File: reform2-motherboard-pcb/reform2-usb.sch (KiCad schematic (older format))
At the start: 85 parts, among them J14 USB_INT2, J17 USB3_A, J5 USB3_A, J6 USB3_A, J9 USB_INT1, U15 TPS2561, U16 TPS2561, U9 TUSB8041IPAPRQ1, Y1 24MHz

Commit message: reform2-motherboard: version D-4 finished; fixes critical D-3 bugs; adds PCIe refclk termination, speaker output filter stage, pcie0 3v3 load switch, imx reset line to lpc, charge current control line to lpc
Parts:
- removed R100, R101, R82, R83, R88, R89, R94, R95: 0, Resistor_SMD:R_0603_1608Metric, symbol Device:R_Small
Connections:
- net USB3_1_EN: now also U15.5 (EN2)
- net USB3_1_OVERCURn: now also U15.6 (~FAULT2)
- net USB3_2_EN: now also U15.4 (EN1)
- net USB3_2_OVERCURn: now also U15.10 (~FAULT1)
- net USB3_3_EN: now also U16.5 (EN2)
- net USB3_3_OVERCURn: now also U16.6 (~FAULT2)
- net USB3_4_EN: now also U16.4 (EN1)
- net USB3_4_OVERCURn: now also U16.10 (~FAULT1)
- net +1V1 renamed +1V2
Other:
- note removed: "FIXME: this goes nowhere"
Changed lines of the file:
@@
 Sheet 8 9
 Title "MNT Reform 2 USB"
-Date "2020-04-11"
+Date "2020-05-19"
 Rev "2.0D-4"
 Comp "MNT Research GmbH"
@@
 	9600 1600 9900 1600
 Connection ~ 9900 1600
-$Comp
-L power:+1V1 #PWR035
-U 1 1 5D9F2CBF
-P 15450 1750
-F 0 "#PWR035" H 15450 1600 50  0001 C CNN
-F 1 "+1V1" H 15465 1923 50  0000 C CNN
-F 2 "" H 15450 1750 50  0001 C CNN
-F 3 "" H 15450 1750 50  0001 C CNN
-	1    15450 1750
-	1    0    0    -1
-$EndComp
 Wire Wire Line
 	11800 2300 11900 2300
@@
 	13050 1400 13050 1750
 Wire Wire Line
-	15450 1750 15450 1800
-Wire Wire Line
 	13050 1150 13050 1200
 Wire Wire Line
@@
 Text GLabel 7050 5900 2    50   Input ~ 0
 USB_PWR
-$Comp
-L Device:R_Small R89
-U 1 1 5DA29AEA
-P 3000 1900
-F 0 "R89" V 2900 1900 50  0000 C CNN
-F 1 "0" V 3000 1900 50  0000 C CNN
-F 2 "Resistor_SMD:R_0603_1608Metric" H 3000 1900 50  0001 C CNN
-F 3 "~" H 3000 1900 50  0001 C CNN
-F 4 "Vishay Dale" H 3000 1900 50  0001 C CNN "Manufacturer"
-F 5 "CRCW06030000Z0EAC" H 3000 1900 50  0001 C CNN "Manufacturer_No"
-F 6 "Mouser" H 3000 1900 50  0001 C CNN "Distributor"
-F 7 "y" H 3000 1900 50  0001 C CNN "Checked"
-	1    3000 1900
-	0    -1   -1   0
-$EndComp
-$Comp
-L Device:R_Small R88
-U 1 1 5DA2A4B1
-P 3000 1600
-F 0 "R88" V 2900 1600 50  0000 C CNN
-F 1 "0" V 3000 1600 50  0000 C CNN
-F 2 "Resistor_SMD:R_0603_1608Metric" H 3000 1600 50  0001 C CNN
-F 3 "~" H 3000 1600 50  0001 C CNN
-F 4 "Vishay Dale" H 3000 1600 50  0001 C CNN "Manufacturer"
-F 5 "CRCW06030000Z0EAC" H 3000 1600 50  0001 C CNN "Manufacturer_No"
-F 6 "Mouser" H 3000 1600 50  0001 C CNN "Distributor"
-F 7 "y" H 3000 1600 50  0001 C CNN "Checked"
-	1    3000 1600
-	0    -1   -1   0
-$EndComp
-$Comp
-L Device:R_Small R100
-U 1 1 5DA2A6C7
-P 6500 1600
-F 0 "R100" V 6400 1600 50  0000 C CNN
-F 1 "0" V 6500 1600 50  0000 C CNN
-F 2 "Resistor_SMD:R_0603_1608Metric" H 6500 1600 50  0001 C CNN
-F 3 "~" H 6500 1600 50  0001 C CNN
-F 4 "Vishay Dale" H 6500 1600 50  0001 C CNN "Manufacturer"
-F 5 "CRCW06030000Z0EAC" H 6500 1600 50  0001 C CNN "Manufacturer_No"
-F 6 "Mouser" H 6500 1600 50  0001 C CNN "Distributor"
-F 7 "y" H 6500 1600 50  0001 C CNN "Checked"
-	1    6500 1600
-	0    -1   -1   0
-$EndComp
-$Comp
-L Device:R_Small R101
-U 1 1 5DA2AAEE
-P 6500 1900
-F 0 "R101" V 6400 1900 50  0000 C CNN
-F 1 "0" V 6500 1900 50  0000 C CNN
-F 2 "Resistor_SMD:R_0603_1608Metric" H 6500 1900 50  0001 C CNN
-F 3 "~" H 6500 1900 50  0001 C CNN
-F 4 "Vishay Dale" H 6500 1900 50  0001 C CNN "Manufacturer"
-F 5 "CRCW06030000Z0EAC" H 6500 1900 50  0001 C CNN "Manufacturer_No"
-F 6 "Mouser" H 6500 1900 50  0001 C CNN "Distributor"
-F 7 "y" H 6500 1900 50  0001 C CNN "Checked"
-	1    6500 1900
-	0    -1   -1   0
-$EndComp
 Text GLabel 13500 3500 2    50   Input ~ 0
 USB3_1_OVERCURn
@@
 Text GLabel 13500 6200 2    50   Input ~ 0
 USB3_4_OVERCURn
-Text GLabel 3100 1900 2    50   Output ~ 0
+Text GLabel 2900 1900 2    50   Output ~ 0
 USB3_1_OVERCURn
-Text GLabel 3100 1600 2    50   Output ~ 0
+Text GLabel 2900 1600 2    50   Output ~ 0
 USB3_2_OVERCURn
 Text GLabel 2100 6700 2    50   Output ~ 0
@@
 Wire Wire Line
 	5700 2450 5700 2400
-Wire Wire Line
-	1450 1800 1700 1800
-Wire Wire Line
-	1700 1900 1450 1900
 $Comp
 L Device:C_Small C66
@@
 Wire Wire Line
 	1550 6200 1800 6200
-Text GLabel 6600 1900 2    50   Output ~ 0
+Text GLabel 6400 1900 2    50   Output ~ 0
 USB3_3_OVERCURn
-Text GLabel 6600 1600 2    50   Output ~ 0
+Text GLabel 6400 1600 2    50   Output ~ 0
 USB3_4_OVERCURn
 $Comp
@@
 	10300 5200 10900 5200
 Wire Wire Line
-	5200 1800 4800 1800
-Wire Wire Line
-	4800 1900 5200 1900
-Wire Wire Line
 	4900 2200 4900 1600
 Connection ~ 4900 1600
@@
 	4900 2450 4900 2400
 Connection ~ 5700 2450
-$Comp
-L Device:R_Small R82
-U 1 1 5DC331BA
-P 1350 1800
-F 0 "R82" V 1250 1800 50  0000 C CNN
-F 1 "0" V 1350 1800 50  0000 C CNN
-F 2 "Resistor_SMD:R_0603_1608Metric" H 1350 1800 50  0001 C CNN
-F 3 "~" H 1350 1800 50  0001 C CNN
-F 4 "Vishay Dale" H 1350 1800 50  0001 C CNN "Manufacturer"
-F 5 "CRCW06030000Z0EAC" H 1350 1800 50  0001 C CNN "Manufacturer_No"
-F 6 "Mouser" H 1350 1800 50  0001 C CNN "Distributor"
-F 7 "y" H 1350 1800 50  0001 C CNN "Checked"
-	1    1350 1800
-	0    1    1    0
-$EndComp
-Wire Wire Line
-	1250 1800 1200 1800
-$Comp
-L Device:R_Small R83
-U 1 1 5DC3CB0C
-P 1350 1900
-F 0 "R83" V 1250 1900 50  0000 C CNN
-F 1 "0" V 1350 1900 50  0000 C CNN
-F 2 "Resistor_SMD:R_0603_1608Metric" H 1350 1900 50  0001 C CNN
-F 3 "~" H 1350 1900 50  0001 C CNN
-F 4 "Vishay Dale" H 1350 1900 50  0001 C CNN "Manufacturer"
-F 5 "CRCW06030000Z0EAC" H 1350 1900 50  0001 C CNN "Manufacturer_No"
-F 6 "Mouser" H 1350 1900 50  0001 C CNN "Distributor"
-F 7 "y" H 1350 1900 50  0001 C CNN "Checked"
-	1    1350 1900
-	0    -1   -1   0
-$EndComp
-Wire Wire Line
-	1250 1900 1200 1900
-$Comp
-L Device:R_Small R94
-U 1 1 5DC58706
-P 4700 1800
-F 0 "R94" V 4600 1800 50  0000 C CNN
-F 1 "0" V 4700 1800 50  0000 C CNN
-F 2 "Resistor_SMD:R_0603_1608Metric" H 4700 1800 50  0001 C CNN
-F 3 "~" H 4700 1800 50  0001 C CNN
-F 4 "Vishay Dale" H 4700 1800 50  0001 C CNN "Manufacturer"
-F 5 "CRCW06030000Z0EAC" H 4700 1800 50  0001 C CNN "Manufacturer_No"
-F 6 "Mouser" H 4700 1800 50  0001 C CNN "Distributor"
-F 7 "y" H 4700 1800 50  0001 C CNN "Checked"
-	1    4700 1800
-	0    1    1    0
-$EndComp
-$Comp
-L Device:R_Small R95
-U 1 1 5DC58710
-P 4700 1900
-F 0 "R95" V 4600 1900 50  0000 C CNN
-F 1 "0" V 4700 1900 50  0000 C CNN
-F 2 "Resistor_SMD:R_0603_1608Metric" H 4700 1900 50  0001 C CNN
-F 3 "~" H 4700 1900 50  0001 C CNN
-F 4 "Vishay Dale" H 4700 1900 50  0001 C CNN "Manufacturer"
-F 5 "CRCW06030000Z0EAC" H 4700 1900 50  0001 C CNN "Manufacturer_No"
-F 6 "Mouser" H 4700 1900 50  0001 C CNN "Distributor"
-F 7 "y" H 4700 1900 50  0001 C CNN "Checked"
-	1    4700 1900
-	0    -1   -1   0
-$EndComp
-Wire Wire Line
-	4600 1800 4550 1800
-Wire Wire Line
-	4550 1900 4600 1900
 $Comp
 L Device:R_Small R98
@@
 Text Notes 8400 4900 0    50   ~ 0
 TODO: hook up SCL/SDA?
-Text Notes 15000 1200 0    50   ~ 0
-FIXME: this goes nowhere
+$Comp
+L power:+1V2 #PWR0216
+U 1 1 5ECB605D
+P 15450 1700
+F 0 "#PWR0216" H 15450 1550 50  0001 C CNN
+F 1 "+1V2" H 15465 1873 50  0000 C CNN
+F 2 "" H 15450 1700 50  0001 C CNN
+F 3 "" H 15450 1700 50  0001 C CNN
+	1    15450 1700
+	1    0    0    -1
+$EndComp
+Wire Wire Line
+	15450 1700 15450 1800
+Wire Wire Line
+	4550 1800 5200 1800
+Wire Wire Line
+	4550 1900 5200 1900
+Wire Wire Line
+	1200 1800 1700 1800
+Wire Wire Line
+	1200 1900 1700 1900
 $EndSCHEMATC

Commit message: reform2-motherboard: first R-1 snapshot. main changes: EMI, ESD, audio filter, enable FETs, SHDN fix, more rail switches
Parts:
- added C164, C167: 10uF, Capacitor_SMD:C_0603_1608Metric, symbol Device:C_Small
- added R2, R83: 10k, Resistor_SMD:R_0603_1608Metric, symbol Device:R_Small
- added U21, U25, U26: SP3012-06UTG, footprints:SON50P350X135X55-14N, symbol reform2:SP3012-06UTG
- added U24, U27: AP22815, footprints:TSOT-25, symbol reform2:AP22815
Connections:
- net +3V3: now also C167.1, R2.2, U27.5 (IN); no longer FB1.1
- net +5V: now also C164.1, R83.2, U24.5 (IN); no longer C43.1, C66.1, C73.1, FB8.1, R61.2, U15.2 (IN), U15.3 (IN), U16.2 (IN), U16.3 (IN)
- net GND: now also C164.2, C167.2, U21.10, U21.5, U24.2 (GND), U25.10, U25.5, U26.10, U26.5, U27.2 (GND)
- net USB2_DN: now also U21.12, U21.3
- net USB2_DP: now also U21.11, U21.4
- net USB2_RX_N: now also U21.7, U21.8
- net USB2_RX_P: now also U21.6, U21.9
- net USB2_TX_N: now also U21.13, U21.2
- net USB2_TX_P: now also U21.1, U21.14
- net USB3_1_DN: now also U25.12, U25.3
- net USB3_1_DP: now also U25.11, U25.4
- net USB3_1_SSRXN: now also U25.7, U25.8
- net USB3_1_SSRXP: now also U25.6, U25.9
- net USB3_2_DN: now also U26.12, U26.3
- net USB3_2_DP: now also U26.11, U26.4
- net USB3_2_SSRXN: now also U26.7, U26.8
- net USB3_2_SSRXP: now also U26.6, U26.9
- net USB3_1_SSTXCN: now reaches C40.2, J6.8 (SSTX-)
- net USB3_1_SSTXCN: now also U25.13, U25.2
- net USB3_1_SSTXCP: now reaches C42.2, J6.9 (SSTX+)
- net USB3_1_SSTXCP: now also U25.1, U25.14
- net USB3_2_SSTXCN: now reaches C39.2, J5.8 (SSTX-)
- net USB3_2_SSTXCN: now also U26.13, U26.2
- net USB3_2_SSTXCP: now reaches C41.2, J5.9 (SSTX+)
- net USB3_2_SSTXCP: now also U26.1, U26.14
- new net: R83.1, U24.3 (FLG)
- new net: R2.1, U27.3 (FLG)
- new net 3V3_PWR_AUX: FB1.1, U27.1 (OUT)
- new net AUX_PWR_EN: U27.4 (EN)
- new net USB_PWR: C43.1, C66.1, C73.1, FB8.1, R61.2, U15.2 (IN), U15.3 (IN), U16.2 (IN), U16.3 (IN), U24.1 (OUT)
- new net USB_PWR_EN: U24.4 (EN)
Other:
- note added: "TODO: RESETn pulldown"
- note removed: "TODO: consider ESD7016"
- moved on the sheet: C39, C40, C41, C42, C43, C69, C71, C75, C76, C77, C79, FB6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

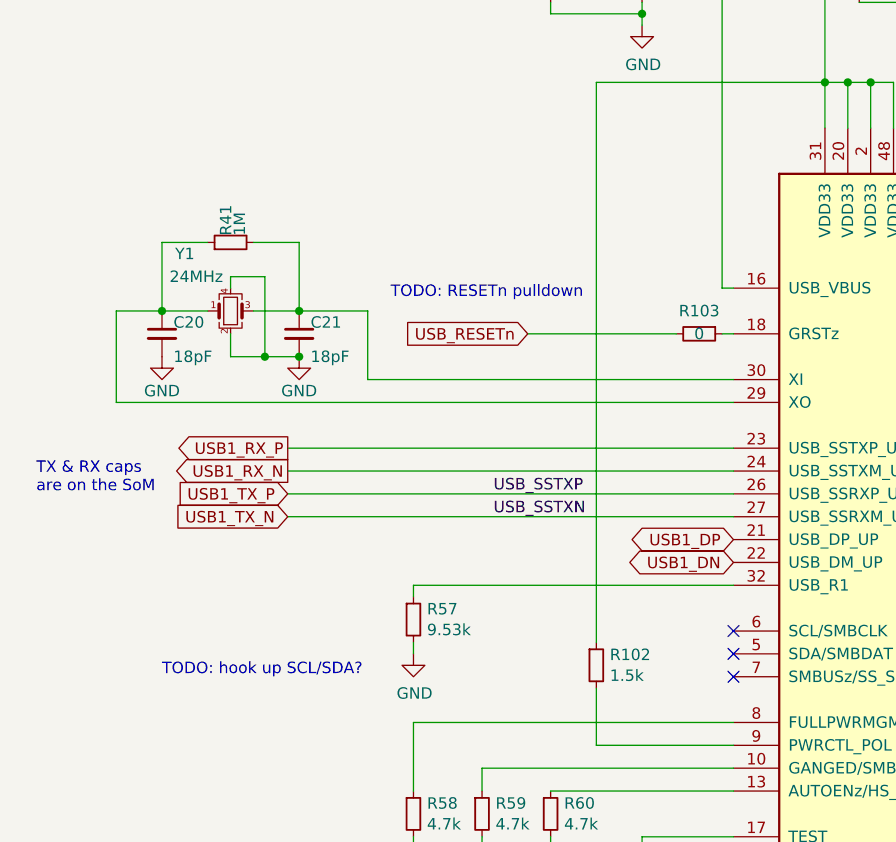
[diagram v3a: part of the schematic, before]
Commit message: reform2-motherboard: R-1 silkscreen cleanup; usb hub reset pulldown added
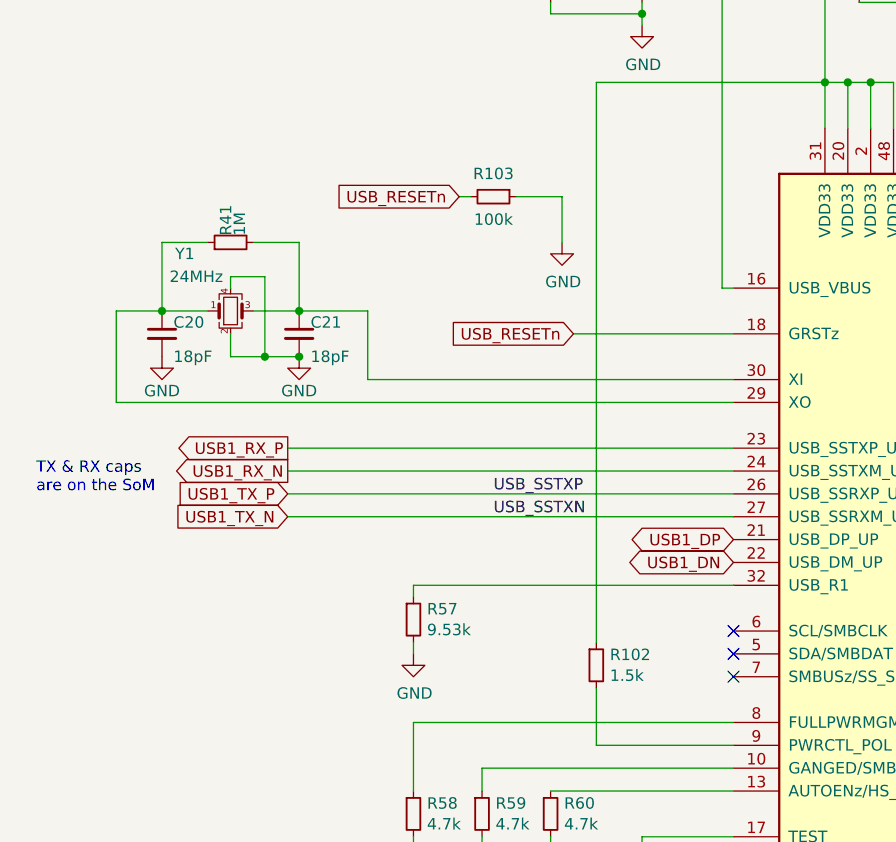
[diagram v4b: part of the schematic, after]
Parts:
- R103: value 0 -> 100k
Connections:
- net GND: now also R103.1
- net USB_RESETn: now also U9.18 (GRSTz)
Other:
- note removed: "TODO: RESETn pulldown"
- note removed: "TODO: hook up SCL/SDA?"
- moved on the sheet: R103
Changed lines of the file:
@@
 Text GLabel 5500 6500 2    50   Input ~ 0
 USB2_RX_P
-Wire Wire Line
-	10850 3400 10900 3400
-Text GLabel 10000 3400 0    50   Input ~ 0
+Text GLabel 10200 3400 0    50   Input ~ 0
 USB_RESETn
-Wire Wire Line
-	10000 3400 10650 3400
 Text GLabel 6400 1800 2    50   Output ~ 0
 USB3_3_VBUS
@@
 Wire Wire Line
 	1200 1900 1700 1900
-Text Notes 9400 3250 0    50   ~ 0
-TODO: RESETn pulldown
 Wire Wire Line
 	4950 8600 5350 8600
@@
 L Device:R_Small R103
 U 1 1 5D907271
-P 10750 3400
-F 0 "R103" V 10650 3400 50  0000 C CNN
-F 1 "0" V 10750 3400 50  0000 C CNN
-F 2 "Resistor_SMD:R_0603_1608Metric" H 10750 3400 50  0001 C CNN
-F 3 "~" H 10750 3400 50  0001 C CNN
-F 4 "Vishay Dale" H 10750 3400 50  0001 C CNN "Manufacturer"
-F 5 "CRCW06030000Z0EAC" H 10750 3400 50  0001 C CNN "Manufacturer_No"
-F 6 "Mouser" H 10750 3400 50  0001 C CNN "Distributor"
-F 7 "y" H 10750 3400 50  0001 C CNN "Checked"
-	1    10750 3400
+P 9850 2800
+F 0 "R103" V 9750 2800 50  0000 C CNN
+F 1 "100k" V 9950 2800 50  0000 C CNN
+F 2 "Resistor_SMD:R_0603_1608Metric" H 9850 2800 50  0001 C CNN
+F 3 "~" H 9850 2800 50  0001 C CNN
+F 4 "Vishay Dale" H 9850 2800 50  0001 C CNN "Manufacturer"
+F 5 "CRCW06030000Z0EAC" H 9850 2800 50  0001 C CNN "Manufacturer_No"
+F 6 "Mouser" H 9850 2800 50  0001 C CNN "Distributor"
+F 7 "y" H 9850 2800 50  0001 C CNN "Checked"
+	1    9850 2800
 	0    1    1    0
 $EndComp
@@
 	1    0    0    -1
 $EndComp
-Text Notes 8400 4900 0    50   ~ 0
-TODO: hook up SCL/SDA?
 Text GLabel 4900 1400 1    50   Input ~ 0
 USB_PWR
@@
 Wire Wire Line
 	12900 900  13050 900
+Wire Wire Line
+	10200 3400 10900 3400
+$Comp
+L power:GND #PWR0124
+U 1 1 64BF7D92
+P 10150 3000
+F 0 "#PWR0124" H 10150 2750 50  0001 C CNN
+F 1 "GND" H 10155 2827 50  0000 C CNN
+F 2 "" H 10150 3000 50  0001 C CNN
+F 3 "" H 10150 3000 50  0001 C CNN
+	1    10150 3000
+	1    0    0    -1
+$EndComp
+Text GLabel 9700 2800 0    50   Input ~ 0
+USB_RESETn
+Wire Wire Line
+	9700 2800 9750 2800
+Wire Wire Line
+	9950 2800 10150 2800
+Wire Wire Line
+	10150 2800 10150 3000
 $EndSCHEMATC

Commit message: motherboard: r-1 release snapshot
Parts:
- removed R98: 0, Resistor_SMD:R_0603_1608Metric, symbol Device:R_Small
- J17, J5, J6: footprint Connector_USB:USB3_A_Molex_48393-001 -> footprints:692121030100; Manufacturer Molex -> Wuerth; Manufacturer_No 48393-0003 -> 692121030100
- R103: Manufacturer_No CRCW06030000Z0EAC -> CRCW0603100KJNEAC
- U21, U25, U26: Distributor (none) -> Mouser; Manufacturer (none) -> Littelfuse; Manufacturer_No (none) -> SP3012-06UTG
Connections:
- net at J17.1 (VBUS): now also C72.1, C84.1, FB8.2
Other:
- note added: "TODO: these reverse leak into AUX_PWR_3V3"
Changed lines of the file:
@@
 Sheet 8 9
 Title "MNT Reform 2 USB"
-Date "2020-05-19"
-Rev "2.0D-4"
+Date "2020-09-24"
+Rev "2.0R-1"
 Comp "MNT Research GmbH"
 Comment1 "https://mntre.com"
@@
 Connection ~ 5700 2450
 Wire Wire Line
-	5500 5900 5600 5900
-Wire Wire Line
 	2550 3450 2550 3400
 Connection ~ 2550 3400
@@
 	6450 6200 6450 6150
 Wire Wire Line
-	5900 5900 6050 5900
-Wire Wire Line
 	1350 4500 1450 4500
 Connection ~ 1450 4500
@@
 Wire Wire Line
 	6750 5900 6850 5900
-$Comp
-L power:PWR_FLAG #FLG0114
-U 1 1 649889EB
-P 5600 5900
-F 0 "#FLG0114" H 5600 5975 50  0001 C CNN
-F 1 "PWR_FLAG" H 5600 6073 50  0000 C CNN
-F 2 "" H 5600 5900 50  0001 C CNN
-F 3 "~" H 5600 5900 50  0001 C CNN
-	1    5600 5900
-	1    0    0    -1
-$EndComp
-Connection ~ 5600 5900
-Wire Wire Line
-	5600 5900 5700 5900
 Wire Wire Line
 	8700 3400 8700 3500
@@
 F 0 "J5" H 5057 4517 50  0000 C CNN
 F 1 "USB3_A" H 5057 4426 50  0000 C CNN
-F 2 "Connector_USB:USB3_A_Molex_48393-001" H 5150 3900 50  0001 C CNN
+F 2 "footprints:692121030100" H 5150 3900 50  0001 C CNN
 F 3 "~" H 5150 3900 50  0001 C CNN
-F 4 "Molex" H 5000 3800 50  0001 C CNN "Manufacturer"
-F 5 "48393-0003" H 5000 3800 50  0001 C CNN "Manufacturer_No"
+F 4 "Wuerth" H 5000 3800 50  0001 C CNN "Manufacturer"
+F 5 "692121030100" H 5000 3800 50  0001 C CNN "Manufacturer_No"
 F 6 "y" H 5000 3800 50  0001 C CNN "Checked"
 F 7 "Mouser" H 5000 3800 50  0001 C CNN "Distributor"
@@
 F 44 "" H 13700 9150 50  0001 L BNN "Field44"
 F 45 "" H 13700 9150 50  0001 L BNN "Field45"
+F 46 "Mouser" H 14150 8500 50  0001 C CNN "Distributor"
+F 47 "Littelfuse" H 14150 8500 50  0001 C CNN "Manufacturer"
+F 48 "SP3012-06UTG" H 14150 8500 50  0001 C CNN "Manufacturer_No"
 	1    14150 8500
 	1    0    0    -1
@@
 F 44 "" H 11200 9150 50  0001 L BNN "Field44"
 F 45 "" H 11200 9150 50  0001 L BNN "Field45"
+F 46 "Mouser" H 11650 8500 50  0001 C CNN "Distributor"
+F 47 "Littelfuse" H 11650 8500 50  0001 C CNN "Manufacturer"
+F 48 "SP3012-06UTG" H 11650 8500 50  0001 C CNN "Manufacturer_No"
 	1    11650 8500
 	1    0    0    -1
@@
 F 44 "" H 8850 9150 50  0001 L BNN "Field44"
 F 45 "" H 8850 9150 50  0001 L BNN "Field45"
+F 46 "Mouser" H 9300 8500 50  0001 C CNN "Distributor"
+F 47 "Littelfuse" H 9300 8500 50  0001 C CNN "Manufacturer"
+F 48 "SP3012-06UTG" H 9300 8500 50  0001 C CNN "Manufacturer_No"
 	1    9300 8500
 	1    0    0    -1
@@
 $EndComp
 $Comp
-L Device:R_Small R98
-U 1 1 5DC767AD
-P 5800 5900
-F 0 "R98" V 5700 5900 50  0000 C CNN
-F 1 "0" V 5800 5900 50  0000 C CNN
-F 2 "Resistor_SMD:R_0603_1608Metric" H 5800 5900 50  0001 C CNN
-F 3 "~" H 5800 5900 50  0001 C CNN
-F 4 "Vishay Dale" H 5800 5900 50  0001 C CNN "Manufacturer"
-F 5 "CRCW06030000Z0EAC" H 5800 5900 50  0001 C CNN "Manufacturer_No"
-F 6 "Mouser" H 5800 5900 50  0001 C CNN "Distributor"
-F 7 "y" H 5800 5900 50  0001 C CNN "Checked"
-	1    5800 5900
-	0    1    1    0
-$EndComp
-$Comp
 L Device:R_Small R102
 U 1 1 5DBAC04C
@@
 F 0 "J17" H 5057 7017 50  0000 C CNN
 F 1 "USB3_A" H 5057 6926 50  0000 C CNN
-F 2 "Connector_USB:USB3_A_Molex_48393-001" H 5150 6400 50  0001 C CNN
+F 2 "footprints:692121030100" H 5150 6400 50  0001 C CNN
 F 3 "~" H 5150 6400 50  0001 C CNN
-F 4 "Molex" H 5000 6300 50  0001 C CNN "Manufacturer"
-F 5 "48393-0003" H 5000 6300 50  0001 C CNN "Manufacturer_No"
+F 4 "Wuerth" H 5000 6300 50  0001 C CNN "Manufacturer"
+F 5 "692121030100" H 5000 6300 50  0001 C CNN "Manufacturer_No"
 F 6 "y" H 5000 6300 50  0001 C CNN "Checked"
 F 7 "Mouser" H 5000 6300 50  0001 C CNN "Distributor"
@@
 F 3 "~" H 9850 2800 50  0001 C CNN
 F 4 "Vishay Dale" H 9850 2800 50  0001 C CNN "Manufacturer"
-F 5 "CRCW06030000Z0EAC" H 9850 2800 50  0001 C CNN "Manufacturer_No"
+F 5 "CRCW0603100KJNEAC" H 9850 2800 50  0001 C CNN "Manufacturer_No"
 F 6 "Mouser" H 9850 2800 50  0001 C CNN "Distributor"
 F 7 "y" H 9850 2800 50  0001 C CNN "Checked"
@@
 F 0 "J6" H 1507 4517 50  0000 C CNN
 F 1 "USB3_A" H 1507 4426 50  0000 C CNN
-F 2 "Connector_USB:USB3_A_Molex_48393-001" H 1600 3900 50  0001 C CNN
+F 2 "footprints:692121030100" H 1600 3900 50  0001 C CNN
 F 3 "~" H 1600 3900 50  0001 C CNN
-F 4 "Molex" H 1450 3800 50  0001 C CNN "Manufacturer"
-F 5 "48393-0003" H 1450 3800 50  0001 C CNN "Manufacturer_No"
+F 4 "Wuerth" H 1450 3800 50  0001 C CNN "Manufacturer"
+F 5 "692121030100" H 1450 3800 50  0001 C CNN "Manufacturer_No"
 F 6 "y" H 1450 3800 50  0001 C CNN "Checked"
 F 7 "Mouser" H 1450 3800 50  0001 C CNN "Distributor"
@@
 Wire Wire Line
 	10150 2800 10150 3000
+Wire Wire Line
+	5500 5900 6050 5900
+Text Notes 1500 6050 0    50   ~ 0
+TODO: these reverse leak into AUX_PWR_3V3
 $EndSCHEMATC
